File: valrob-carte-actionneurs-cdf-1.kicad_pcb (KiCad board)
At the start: 4 copper layers, 141 parts, among them J1 USB_C_Receptacle_USB2.0_14P, J2 Conn_01x02, J3 Conn_01x02, J4 Conn_01x04_Pin, J5 Conn_01x02, J6 Conn_01x02, M1 Motor_Servo, M10 Motor_Servo, M11 Motor_Servo, M12 Motor_Servo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

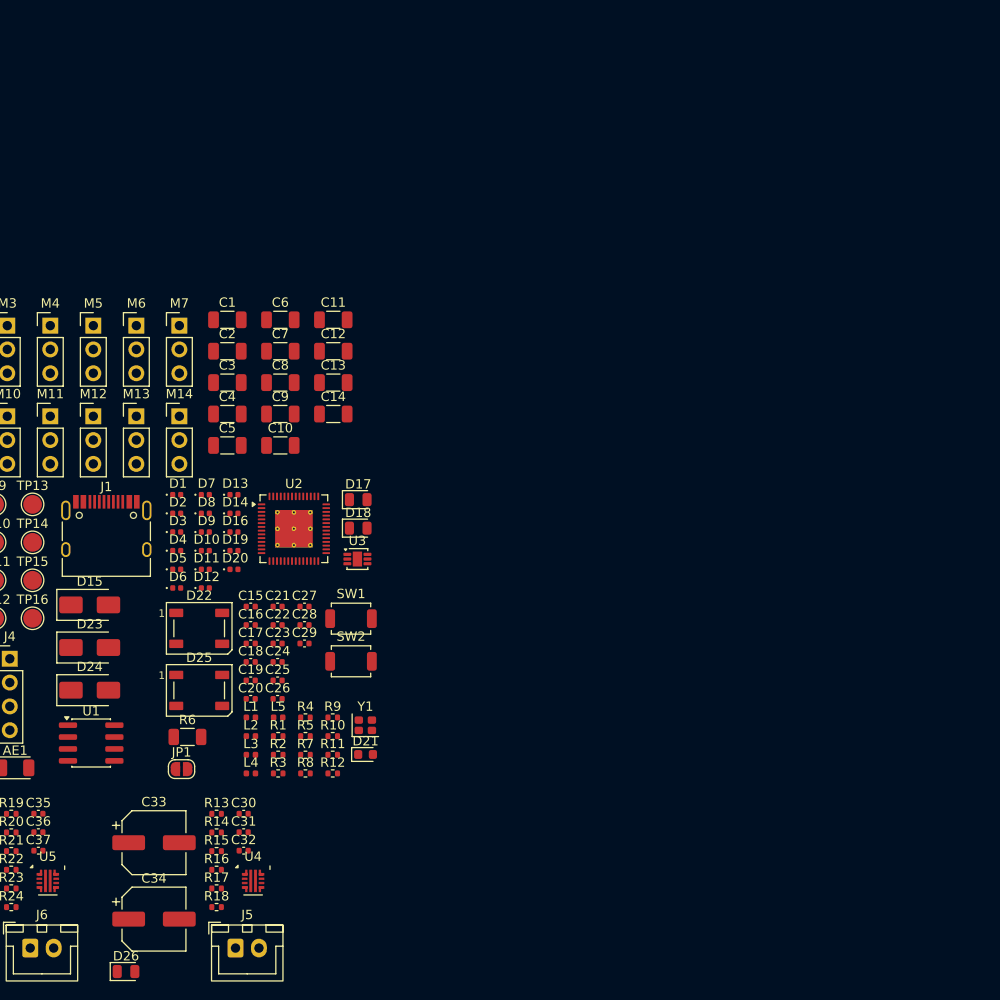
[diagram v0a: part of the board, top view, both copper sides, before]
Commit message: schem/pcb: use TPS efuses ORing configuration
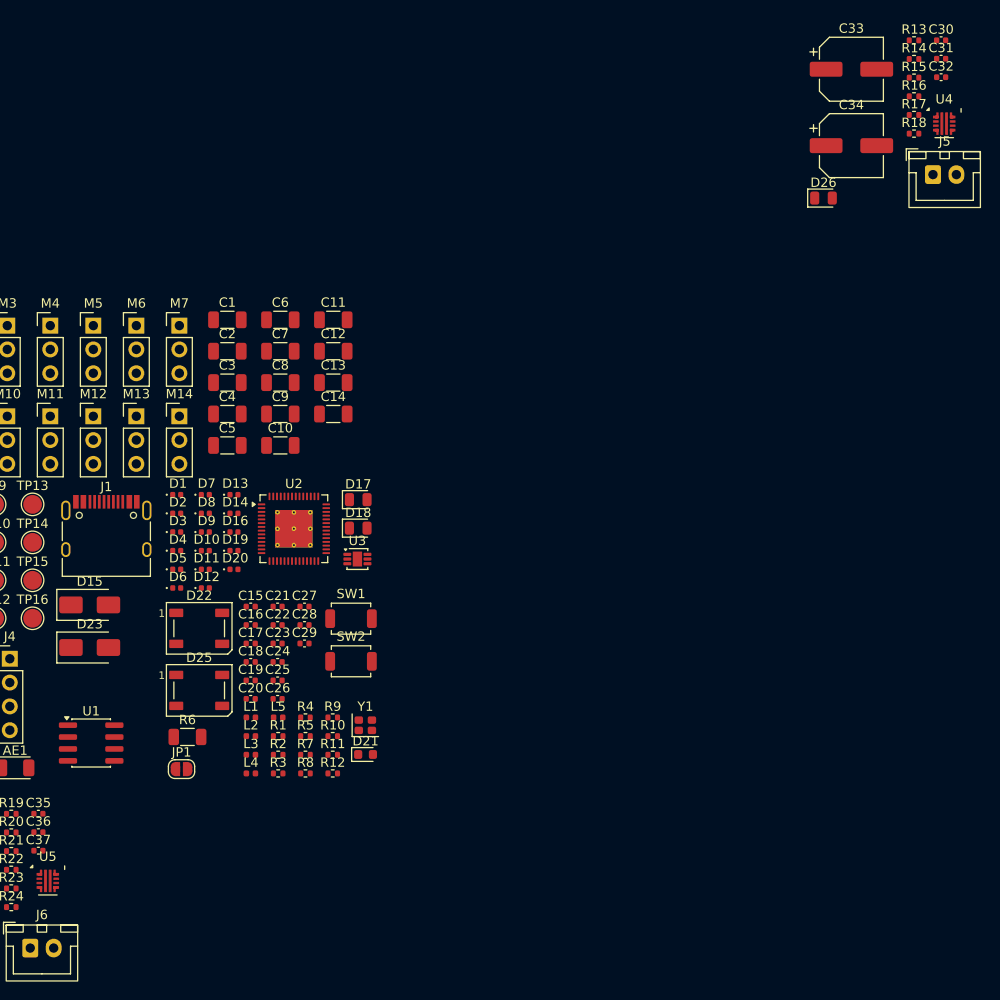
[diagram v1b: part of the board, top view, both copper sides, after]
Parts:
- removed D24: D_Schottky, Diode_SMD:D_SMA
- moved C32 111.1 mm to (136.8, 91.3)
- moved C30 111.1 mm to (136.8, 87.4)
- moved C31 111.1 mm to (136.8, 89.4)
- moved C33 111.1 mm to (127.2, 90.5)
- moved C34 111.1 mm to (127.2, 98.7)
- moved D26 111.1 mm to (124.2, 104.2)
- moved J5 111.1 mm to (135.9, 101.7)
- moved R13 111.1 mm to (133.9, 87.4)
- moved R14 111.1 mm to (133.9, 89.4)
- moved R15 111.1 mm to (133.9, 91.4)
- moved R16 111.1 mm to (133.9, 93.4)
- moved R17 111.1 mm to (133.9, 95.4)
- moved R18 111.1 mm to (133.9, 97.4)
- moved U4 109.4 mm to (137.1, 96.3)
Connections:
- C1 pad 1: +5VA -> +5V
- C10 pad 1: +5VB -> +5V
- C11 pad 1: +5VB -> +5V
- C12 pad 1: +5VB -> +5V
- C13 pad 1: +5VB -> +5V
- C14 pad 1: +5VB -> +5V
- C2 pad 1: +5VA -> +5V
- C3 pad 1: +5VA -> +5V
- C33 pad 1: +5VB -> +5V
- C34 pad 1: +5VB -> +5V
- C38 pad 1: +5VA -> +5V
- C39 pad 1: +5VA -> +5V
- C4 pad 1: +5VA -> +5V
- C5 pad 1: +5VA -> +5V
- C6 pad 1: +5VA -> +5V
- C7 pad 1: +5VA -> +5V
- C8 pad 1: +5VB -> +5V
- C9 pad 1: +5VB -> +5V
- D1 pad 1: +5VA -> +5V
- D10 pad 1: +5VB -> +5V
- D11 pad 1: +5VB -> +5V
- D12 pad 1: +5VB -> +5V
- D13 pad 1: +5VB -> +5V
- D14 pad 1: +5VB -> +5V
- D19 pad 1: +5VB -> +5V
- D2 pad 1: +5VA -> +5V
- D20 pad 1: +5VB -> +5V
- D23 pad 2: +5VA -> +5V
- D3 pad 1: +5VA -> +5V
- D4 pad 1: +5VA -> +5V
- D5 pad 1: +5VA -> +5V
- D6 pad 1: +5VA -> +5V
- D9 pad 1: +5VA -> +5V
- M1 pad 2: +5VA -> +5V
- M10 pad 2: +5VB -> +5V
- M11 pad 2: +5VB -> +5V
- M12 pad 2: +5VB -> +5V
- M13 pad 2: +5VB -> +5V
- M14 pad 2: +5VB -> +5V
- M2 pad 2: +5VA -> +5V
- M3 pad 2: +5VA -> +5V
- M4 pad 2: +5VA -> +5V
- M5 pad 2: +5VA -> +5V
- M6 pad 2: +5VA -> +5V
- M7 pad 2: +5VA -> +5V
- M8 pad 2: +5VB -> +5V
- M9 pad 2: +5VB -> +5V
- R17 pad 2: +5VB -> +5V
- R23 pad 2: +5VA -> +5V
- TP1 pad 1: +5VA -> +5V
- TP10 pad 1: +5VB -> +5V
- TP11 pad 1: +5VB -> +5V
- TP12 pad 1: +5VB -> +5V
- TP13 pad 1: +5VB -> +5V
- TP14 pad 1: +5VB -> +5V
- TP2 pad 1: +5VA -> +5V
- TP3 pad 1: +5VA -> +5V
- TP4 pad 1: +5VA -> +5V
- TP5 pad 1: +5VA -> +5V
- TP6 pad 1: +5VA -> +5V
- TP7 pad 1: +5VA -> +5V
- TP8 pad 1: +5VB -> +5V
- TP9 pad 1: +5VB -> +5V
- U4 pad 6: +5VB -> +5V
- U5 pad 6: +5VA -> +5V

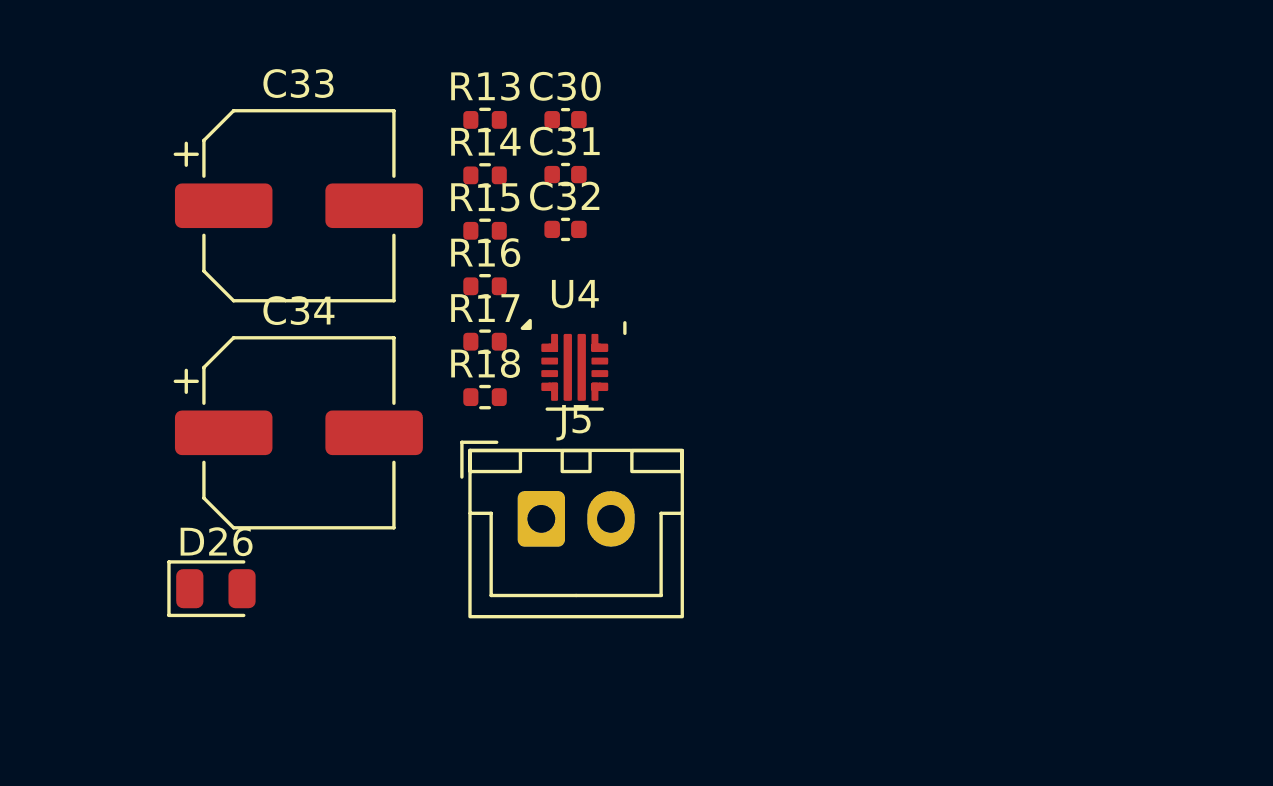
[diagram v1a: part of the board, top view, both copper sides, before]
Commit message: schem: remove 5v input bulk cap
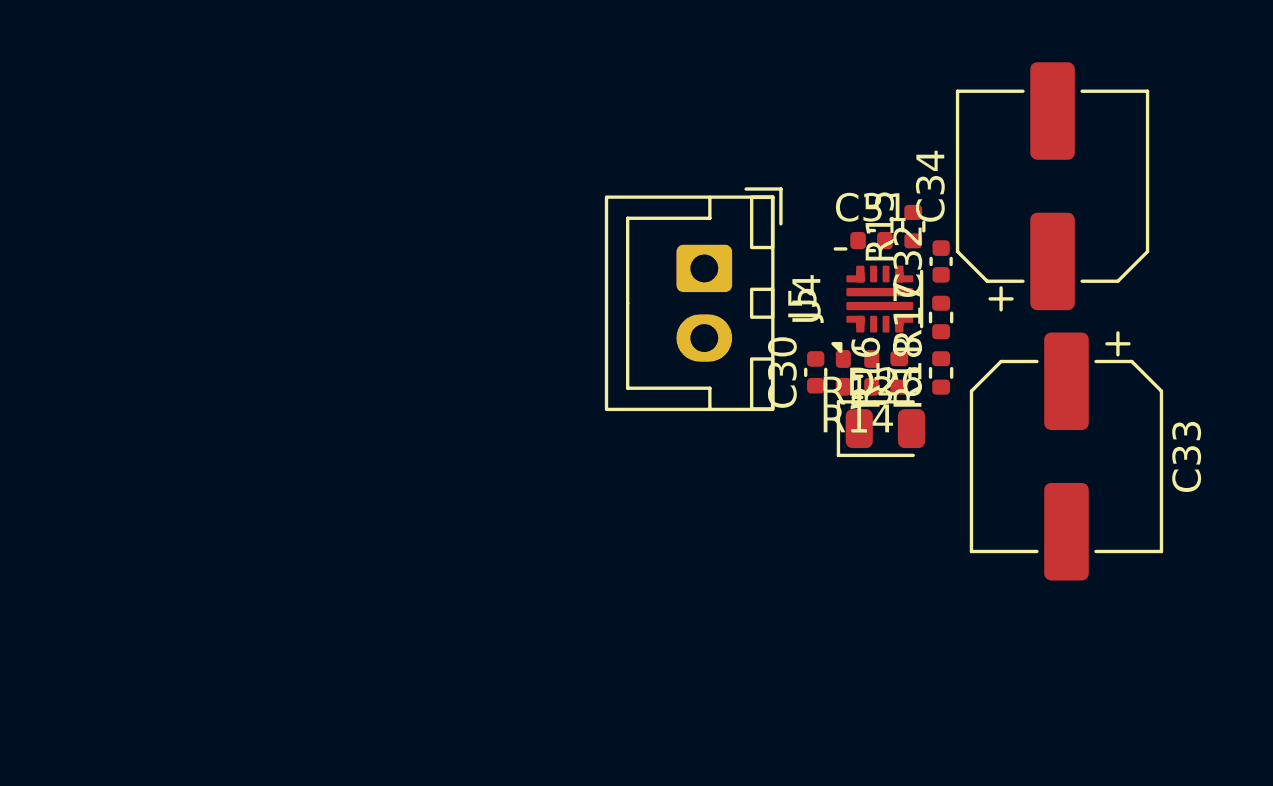
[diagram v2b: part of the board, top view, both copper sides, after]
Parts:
- moved C33 29.0 mm to (154.8, 99.5), turned to -90 degrees
- moved C34 28.5 mm to (154.2, 89.8), turned to 90 degrees
- moved D26 24.7 mm to (148.2, 98.5)
- moved R18 16.4 mm to (150.2, 96.5), turned to 90 degrees
- moved R17 16.4 mm to (150.2, 94.5), turned to 90 degrees
- moved R13 15.9 mm to (147.2, 96.0), turned to 180 degrees
- moved R14 15.4 mm to (147.2, 97.0), turned to 180 degrees
- moved R15 15.4 mm to (149.2, 91.2), turned to 90 degrees
- moved R16 15.2 mm to (148.8, 96.5), turned to 90 degrees
- moved C32 13.5 mm to (150.2, 92.5), turned to 90 degrees
- moved C30 12.8 mm to (145.8, 96.5), turned to 90 degrees
- moved C31 11.2 mm to (147.8, 91.8)
- moved U4 11.2 mm to (148.1, 93.8), turned to 90 degrees
- moved J5 10.7 mm to (141.8, 92.8), turned to -90 degrees

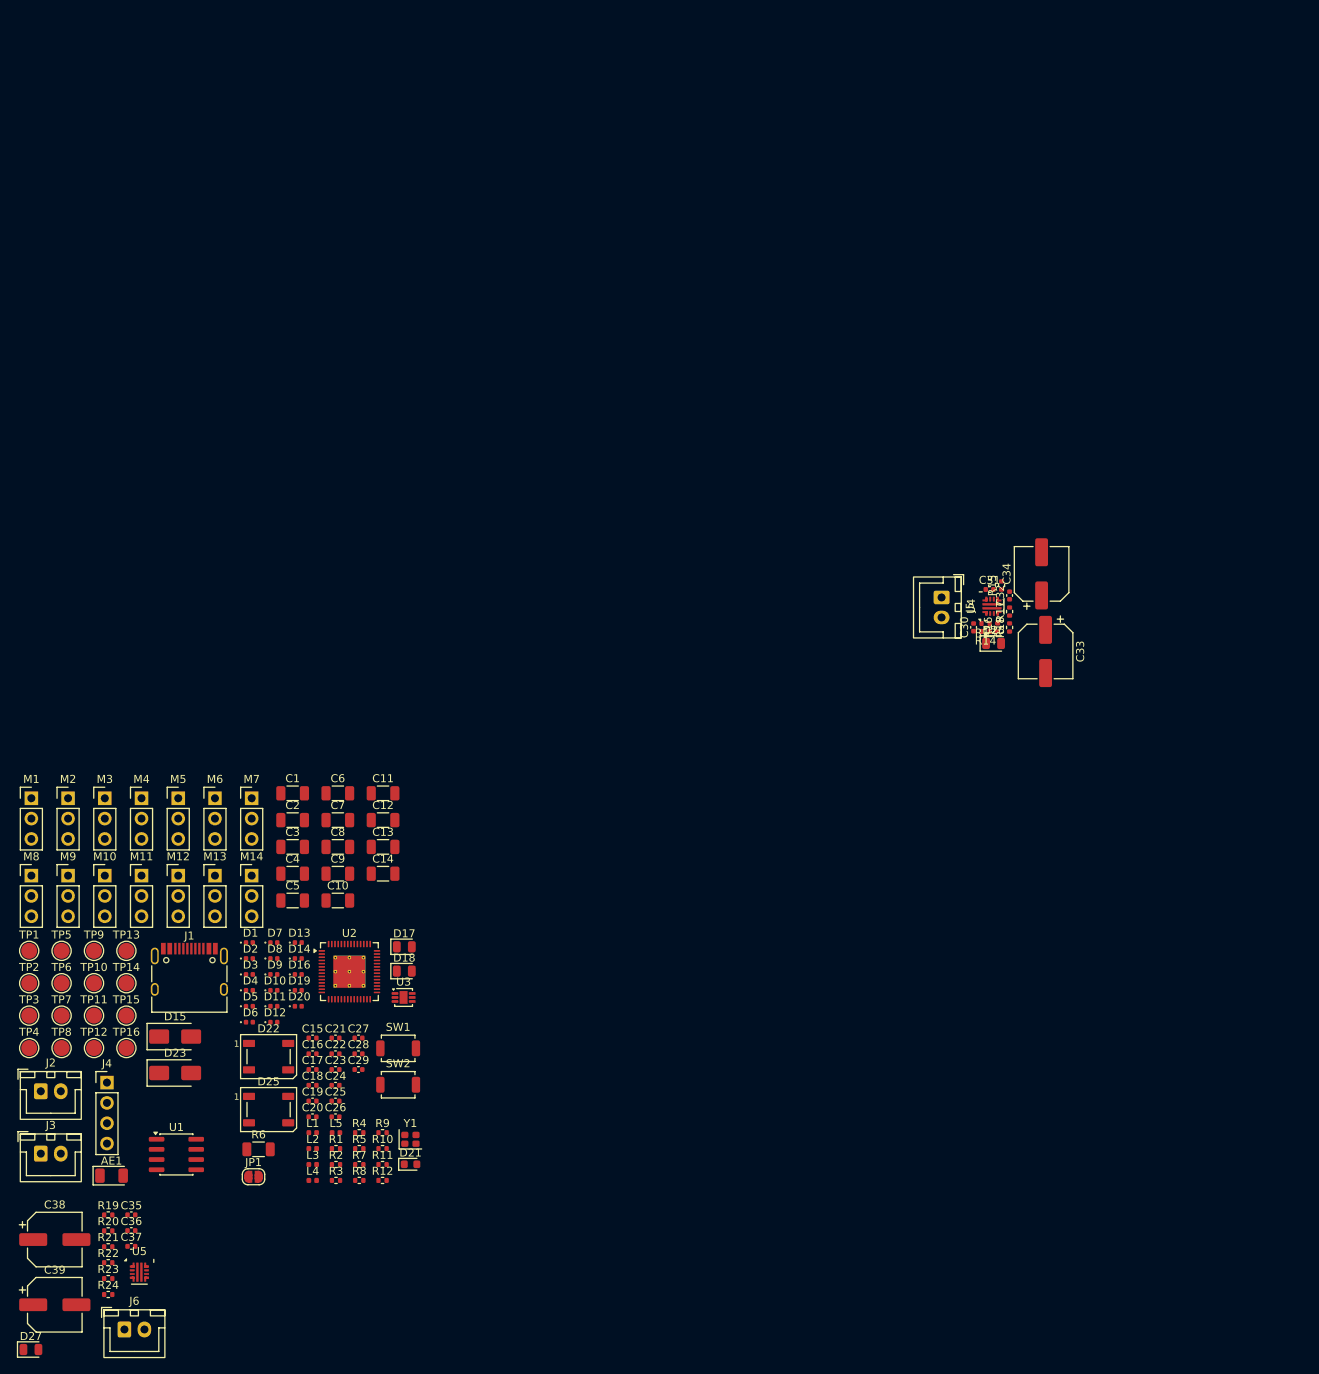
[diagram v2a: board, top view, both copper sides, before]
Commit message: pcb: add 2x TPS25947 layout
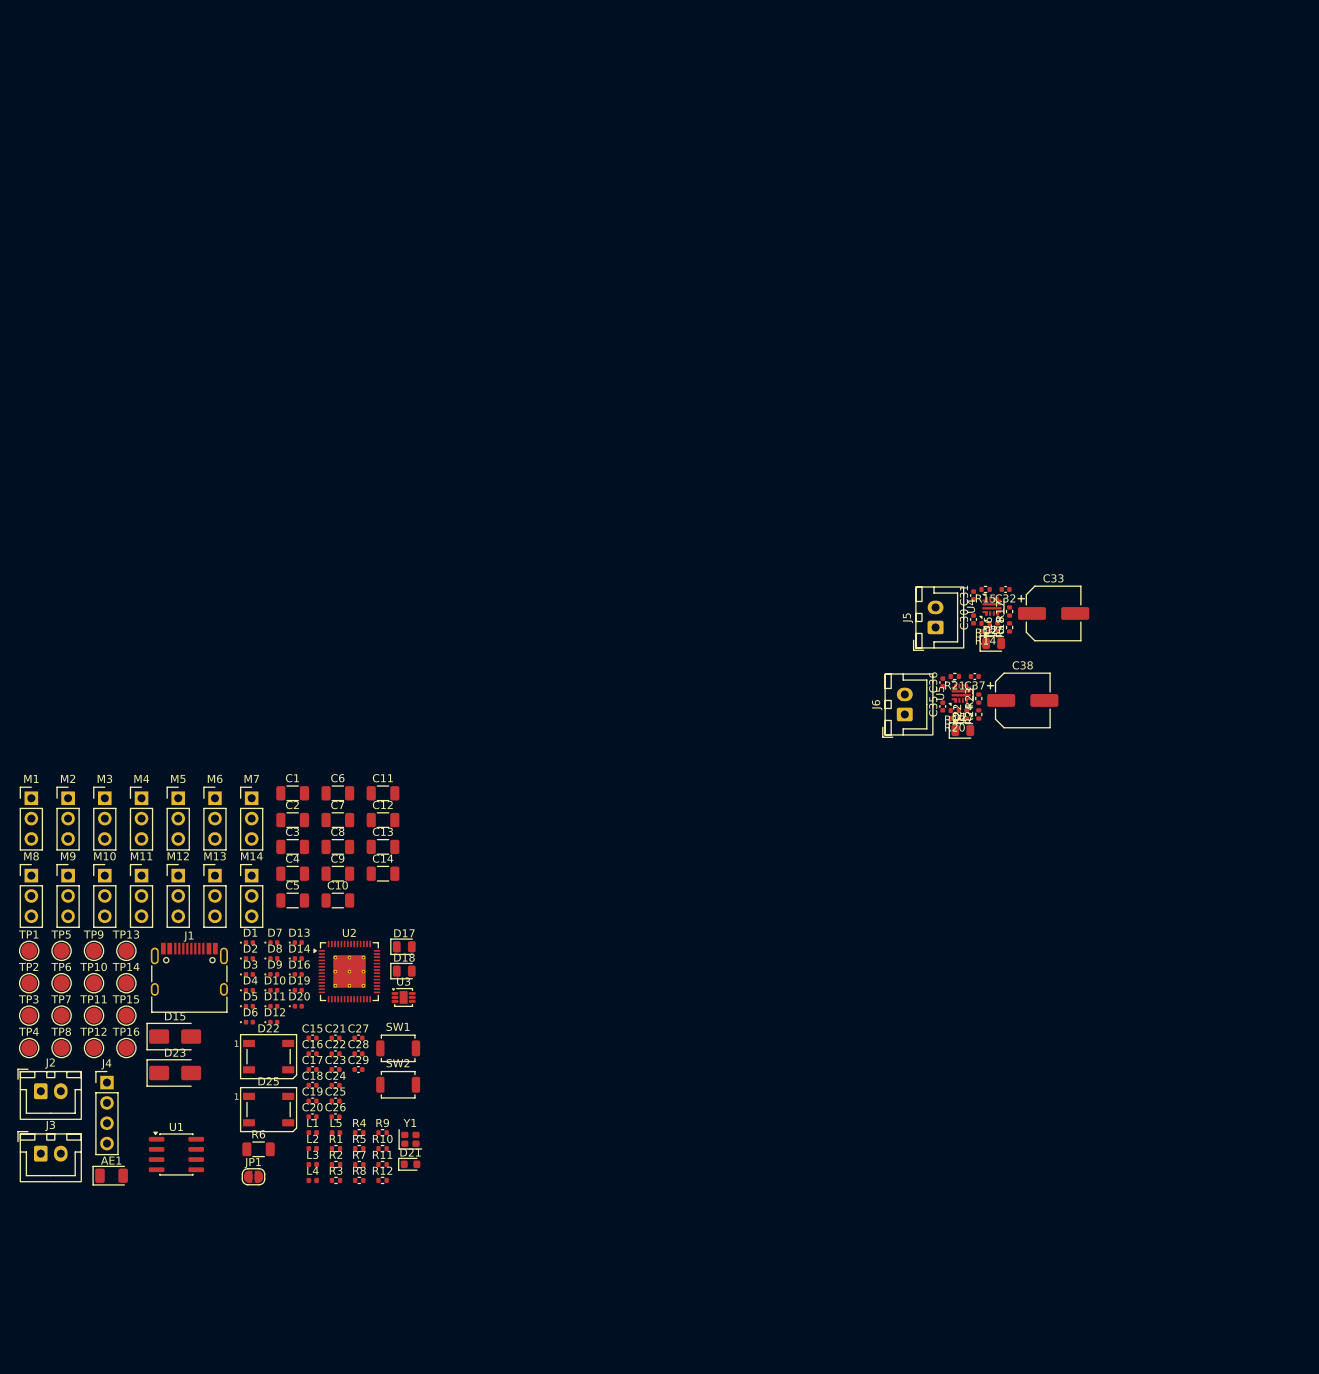
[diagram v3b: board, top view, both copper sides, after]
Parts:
- removed C34, C39: 220u, Capacitor_SMD:CP_Elec_6.3x7.7
- moved D27 139.8 mm to (144.4, 109.4)
- moved C38 138.5 mm to (151.9, 105.6)
- moved R23 130.8 mm to (146.4, 105.4), turned to 90 degrees
- moved R24 130.8 mm to (146.4, 107.4), turned to 90 degrees
- moved R21 127.6 mm to (143.4, 102.6), turned to 180 degrees
- moved R22 127.3 mm to (144.9, 107.4), turned to 90 degrees
- moved C37 127.2 mm to (145.9, 102.6), turned to 180 degrees
- moved U5 125.7 mm to (144.2, 104.7), turned to 90 degrees
- moved J6 124.2 mm to (137.2, 107.4), turned to 90 degrees
- moved R20 123.7 mm to (143.4, 107.9), turned to 180 degrees
- moved R19 123.2 mm to (143.4, 106.9), turned to 180 degrees
- moved C36 122.4 mm to (141.9, 103.4), turned to 90 degrees
- moved C35 119.7 mm to (141.9, 106.4), turned to 90 degrees
- moved C33 4.85 mm to (155.8, 94.8), turned to 0 degrees
- moved J5 3.82 mm to (141.0, 96.5), turned to 90 degrees
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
